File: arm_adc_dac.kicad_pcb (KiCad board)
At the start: 2 copper layers, 13 x 1.4 mm, 18 parts, among them J1 AudioJack2, J2 Conn_01x15, J3 Conn_01x15, P1 USB_C_Plug_USB2.0, U1 STM32F103C8Tx, U2 XC6206PxxxMR, U3 PCM1780, Y1 8MHz

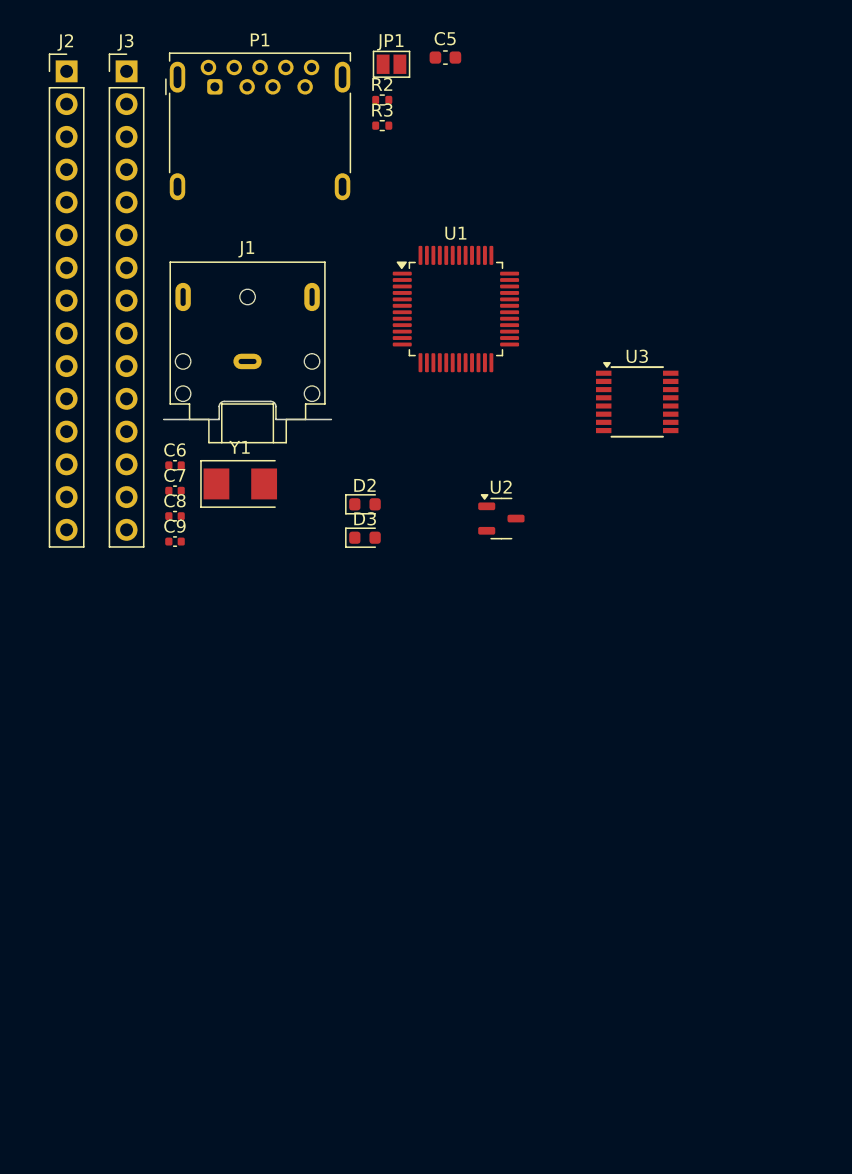
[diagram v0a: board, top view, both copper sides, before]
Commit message: divide the schematic into sub sections, use 12 bit ADC/DAC, add schematic
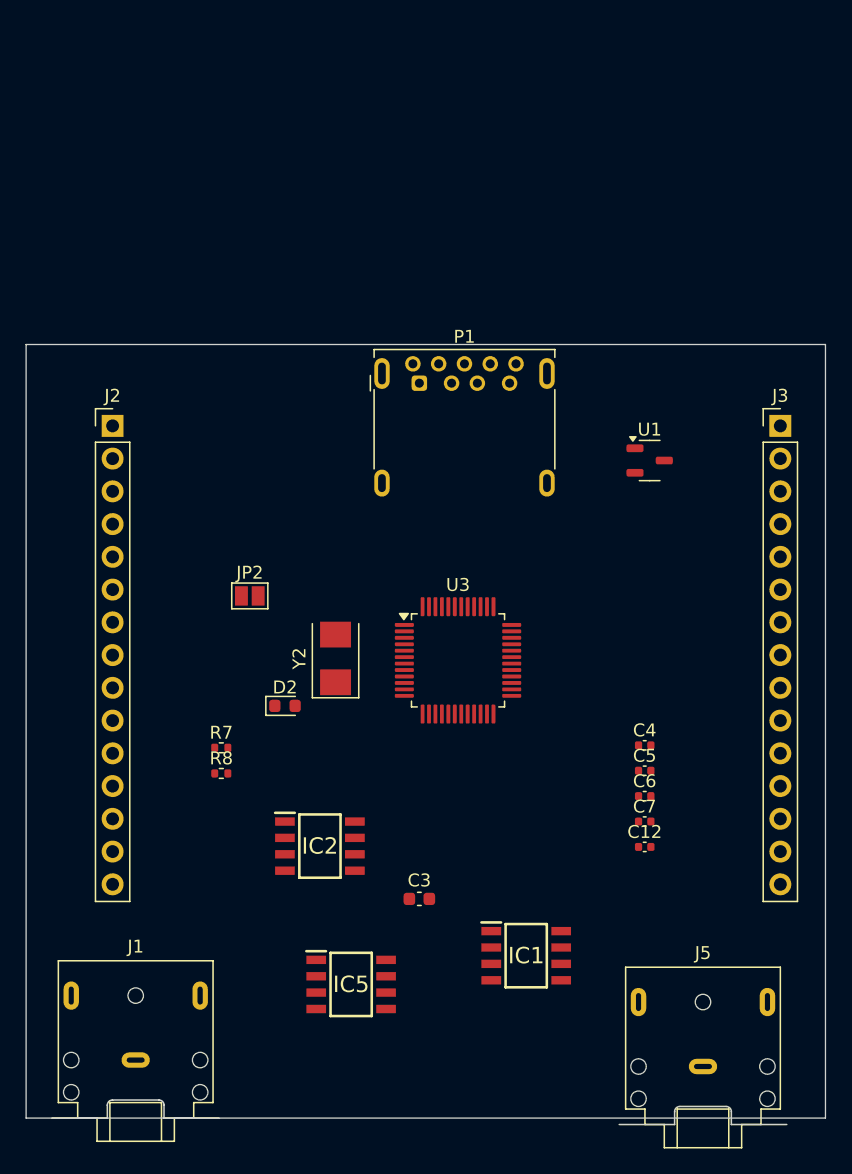
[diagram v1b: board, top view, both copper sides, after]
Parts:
- removed C8, C9: 100n, Capacitor_SMD:C_0402_1005Metric
- removed D3: BLUE, LED_SMD:LED_0603_1608Metric
- removed JP1: SolderJumper_2_Open, Jumper:SolderJumper-2_P1.3mm_Open_Pad1.0x1.5mm
- removed R2, R3: 10k, Resistor_SMD:R_0402_1005Metric
- removed U2: XC6206PxxxMR, Package_TO_SOT_SMD:SOT-23-3
- removed Y1: 8MHz, Crystal:Crystal_SMD_5032-2Pin_5.0x3.2mm
- added C12: 100n, Capacitor_SMD:C_0402_1005Metric, F.Cu at (161.0, 113.0)
- added C3: 4u7, Capacitor_SMD:C_0603_1608Metric, F.Cu at (143.5, 117.0)
- added C4: 100n, Capacitor_SMD:C_0402_1005Metric, F.Cu at (161.0, 105.1)
- added IC1: OPA134UA_2K5, cagil_footprint_library:SOIC127P600X175-8N, F.Cu at (151.8, 121.4)
- added IC2: MCP3201-BI_SN, cagil_footprint_library:SOIC127P600X175-8N, F.Cu at (135.8, 112.9)
- added IC5: OPA134UA_2K5, cagil_footprint_library:SOIC127P600X175-8N, F.Cu at (138.2, 123.6)
- added J5: Output Jack, Connector_Audio:Jack_3.5mm_CUI_SJ1-3523N_Horizontal, F.Cu at (165.5, 130.0)
- added JP2: SolderJumper_2_Open, Jumper:SolderJumper-2_P1.3mm_Open_Pad1.0x1.5mm, F.Cu at (130.3, 93.5)
- added R7: 10k, Resistor_SMD:R_0402_1005Metric, F.Cu at (128.1, 105.3)
- added R8: 10k, Resistor_SMD:R_0402_1005Metric, F.Cu at (128.1, 107.3)
- added Y2: 8MHz, Crystal:Crystal_SMD_5032-2Pin_5.0x3.2mm, F.Cu at (137.0, 98.3)
- C5: value 4u7 -> 100n; footprint Capacitor_SMD:C_0603_1608Metric -> Capacitor_SMD:C_0402_1005Metric
- D2: value GREEN -> BLUE
- J1: value AudioJack2 -> Input Jack
- U1: value STM32F103C8Tx -> XC6206PxxxMR; footprint Package_QFP:LQFP-48_7x7mm_P0.5mm -> Package_TO_SOT_SMD:SOT-23-3
- U3: value PCM1780 -> STM32F103C8Tx; footprint Package_SO:SSOP-16_3.9x4.9mm_P0.635mm -> Package_QFP:LQFP-48_7x7mm_P0.5mm
- moved J3 57.7 mm to (171.5, 80.3)
- moved C5 57.4 mm to (161.0, 107.1)
- moved J1 54.9 mm to (121.5, 129.5)
- moved C6 44.6 mm to (161.0, 109.0)
- moved C7 44.6 mm to (161.0, 111.0)
- moved P1 27.9 mm to (143.5, 77.0)
- moved J2 27.7 mm to (119.7, 80.3)
- moved U3 24.4 mm to (146.5, 98.5)
- moved U1 19.1 mm to (161.4, 83.0)
- moved D2 16.8 mm to (133.1, 102.0)
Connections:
- D2 pad 1: unconnected-(D2-K-Pad1) -> GND
- D2 pad 2: unconnected-(D2-A-Pad2) -> Net-(D2-A)
- J1 pad S: unconnected-(J1-PadS) -> Net-(J1-PadS)
- J3 pad 1: unconnected-(J3-Pin_1-Pad1) -> PA0
- J3 pad 10: unconnected-(J3-Pin_10-Pad10) -> PA9
- J3 pad 11: unconnected-(J3-Pin_11-Pad11) -> PA10
- J3 pad 12: unconnected-(J3-Pin_12-Pad12) -> PA11
- J3 pad 13: unconnected-(J3-Pin_13-Pad13) -> PA12
- J3 pad 14: unconnected-(J3-Pin_14-Pad14) -> PA13
- J3 pad 15: unconnected-(J3-Pin_15-Pad15) -> PA14
- J3 pad 2: unconnected-(J3-Pin_2-Pad2) -> PA1
- J3 pad 3: unconnected-(J3-Pin_3-Pad3) -> PA2
- J3 pad 4: unconnected-(J3-Pin_4-Pad4) -> PA3
- J3 pad 5: unconnected-(J3-Pin_5-Pad5) -> PA4
- J3 pad 6: unconnected-(J3-Pin_6-Pad6) -> PA5
- J3 pad 7: unconnected-(J3-Pin_7-Pad7) -> PA6
- J3 pad 8: unconnected-(J3-Pin_8-Pad8) -> PA7
- J3 pad 9: unconnected-(J3-Pin_9-Pad9) -> PA8
- U1 pad 1: +3.3V -> GND
- U1 pad 2: unconnected-(U1-PC13-Pad2) -> +3.3V
- U1 pad 3: unconnected-(U1-PC14-Pad3) -> VDD
- U3 pad 1: unconnected-(U3-ZEROL-Pad1) -> +3.3V
- U3 pad 10: unconnected-(U3-NC-Pad10) -> PA0
- U3 pad 11: +3V -> PA1
- U3 pad 12: unconnected-(U3-AGND-Pad12) -> PA2
- U3 pad 13: unconnected-(U3-V_{COM}-Pad13) -> SPI_CS_N_ADC
- U3 pad 14: unconnected-(U3-V_{OUT}R-Pad14) -> SPI_CS_N_DAC
- U3 pad 15: unconnected-(U3-V_{OUT}L-Pad15) -> SPI_SCK
- U3 pad 16: unconnected-(U3-ZEROR-Pad16) -> SPI_MISO
- U3 pad 5: unconnected-(U3-SCK-Pad5) -> Net-(U3-PD0)
- U3 pad 6: unconnected-(U3-DATA-Pad6) -> Net-(U3-PD1)
- U3 pad 8: unconnected-(U3-LRCK-Pad8) -> GND
- U3 pad 9: unconnected-(U3-NC-Pad9) -> +3.3VA
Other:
- board size 13 x 1.4 mm -> 62 x 60 mm
